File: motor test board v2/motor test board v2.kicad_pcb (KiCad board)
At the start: 2 copper layers, 78.2 x 49.5 mm, 8 parts, among them J1 Conn_01x02, J2 Conn_01x07, J3 Conn_01x02, U1 MC33887

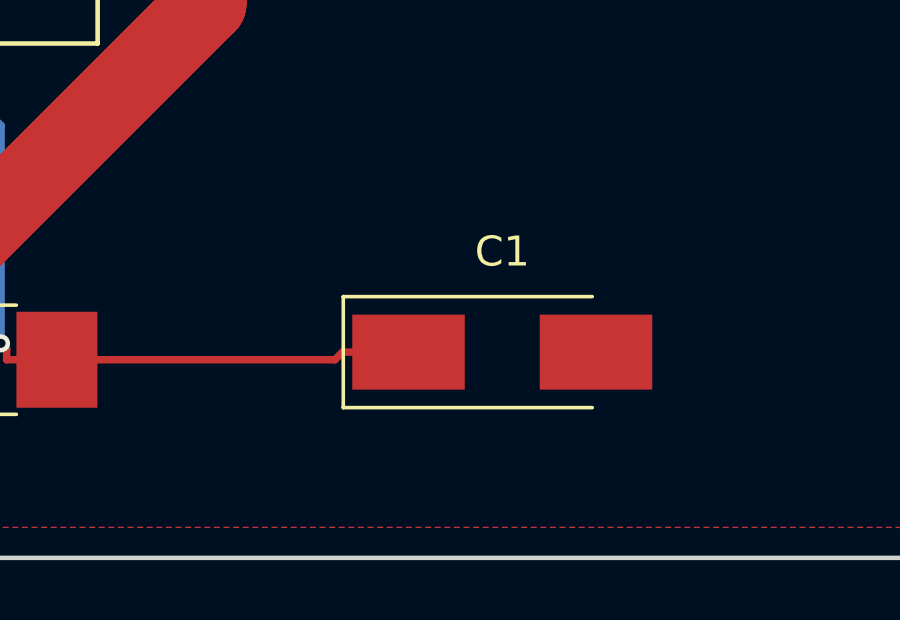
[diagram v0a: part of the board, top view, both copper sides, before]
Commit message: moved cap
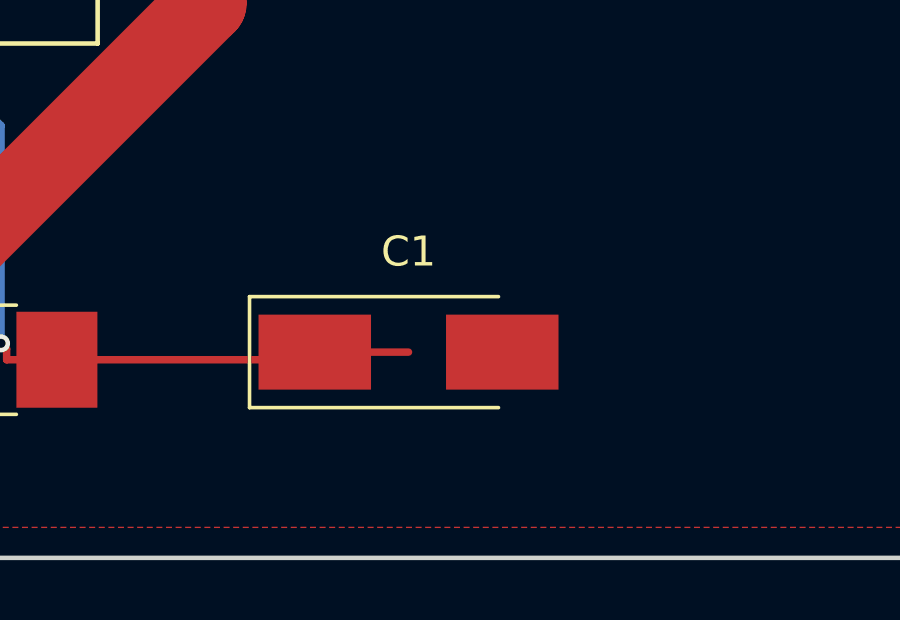
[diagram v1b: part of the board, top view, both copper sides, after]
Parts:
- moved C1 3.12 mm to (186.4, 140.0)
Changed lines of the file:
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@@
   )
   (module Capacitors_Tantalum_SMD:CP_Tantalum_Case-C_EIA-6032-28_Hand (layer F.Cu)
-    (at 189.484 139.954)
+    (at 186.359 139.954)
     (descr "Tantalum capacitor, Case C, EIA 6032-28, 6.0x3.2x2.5mm, Hand soldering footprint")
     (tags "capacitor tantalum smd")
@@
     (connect_pads (clearance 0.508))
     (min_thickness 0.254)
-    (fill yes (arc_segments 16) (thermal_gap 0.508) (thermal_bridge_width 0.508))
+    (fill (arc_segments 16) (thermal_gap 0.508) (thermal_bridge_width 0.508))
     (polygon
       (pts
